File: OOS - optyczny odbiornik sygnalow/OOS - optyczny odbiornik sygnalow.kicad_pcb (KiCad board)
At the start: 2 copper layers, 31 x 47 mm, 55 parts, among them J1 Conn_01x02_Socket, J2 Conn_01x02_Socket, J3 Conn_01x02_Socket, J4 Conn_01x02_Socket, J5 Conn_Coaxial, U1 OPA300AIDBVR, U2 OPA300AIDBVR

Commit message: Creating layout branch, creating a blank pcb file and creating constraints based on JLC PCB capabilities from their website. To every capability lsited a small margin has been added in project constraints (for example if they state min. clearance 0.2mm then in the project that min clearance is 0.3mm
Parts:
- removed C1, C2: 1u, Capacitor_SMD:C_0603_1608Metric
- removed C10, C12: 1p, Capacitor_SMD:C_0402_1005Metric
- removed C11: 100p, Capacitor_SMD:C_0402_1005Metric
- removed C3, C4, C8: 100n, Capacitor_SMD:C_0603_1608Metric
- removed C5, C6, C9: 10n, Capacitor_SMD:C_0402_1005Metric
- removed C7: 2u2, Capacitor_SMD:C_0603_1608Metric
- removed D1, D2: LED, Diode_SMD:D_0603_1608Metric
- removed D3: BPX65, Package_TO_SOT_THT:TO-18-2_Lens
- removed FID1, FID2, FID3: Fiducial, Fiducial:Fiducial_1.5mm_Mask3mm
- removed H1, H2, H3, H4: MountingHole, MountingHole:MountingHole_3.2mm_M3
- removed J1, J2, J3, J4: Conn_01x02_Socket, Connector_PinHeader_2.54mm:PinHeader_1x02_P2.54mm_Vertical
- removed J5: Conn_Coaxial, Connector_Coaxial:BNC_Amphenol_B6252HB-NPP3G-50_Horizontal
- removed JP1: SolderJumper_2_Open, Jumper:SolderJumper-2_P1.3mm_Bridged_RoundedPad1.0x1.5mm
- removed R1: 10k, Resistor_SMD:R_0603_1608Metric
- removed R10, R11, R8: 1k, Resistor_SMD:R_0402_1005Metric
- removed R2: 2k2, Resistor_SMD:R_0603_1608Metric
- removed R3: 10, Resistor_SMD:R_0603_1608Metric
- removed R4, R5, R6, R7: 10k, Resistor_SMD:R_0402_1005Metric
- removed R9: 100, Resistor_SMD:R_0402_1005Metric
- removed REF**: ESD-Logo_6.6x6mm_SilkScreen, Symbol:ESD-Logo_6.6x6mm_SilkScreen
- removed REF**: WEEE-Logo_4.2x6mm_SilkScreen, Symbol:WEEE-Logo_4.2x6mm_SilkScreen
- removed REF**: KiCad-Logo2_5mm_SilkScreen, Symbol:KiCad-Logo2_5mm_SilkScreen
- removed TP1, TP10, TP11, TP2, TP3, TP4, TP5, TP6, TP7, TP8, TP9: TestPoint_Small, TestPoint:TestPoint_Pad_D1.0mm
- removed U1, U2: OPA300AIDBVR, Package_TO_SOT_SMD:SOT-23-6_Handsoldering
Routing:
- net +5V: track 106.5 -> 0.00 mm, vias 2 -> 0
- net /OPA300_En: track 25.1 -> 0.00 mm
- net 0V: track 13.7 -> 0.00 mm, vias 85 -> 0
- net +V_photo: track 9.94 -> 0.00 mm
- net /BPX65_Cathode: track 9.66 -> 0.00 mm
- net /OPA300_TIA_+: track 8.75 -> 0.00 mm
- net /OPA300_TIA_-: track 8.54 -> 0.00 mm
- net /OPA300_En_Alt_Con: track 7.43 -> 0.00 mm
- net /OPA300_x10_Out_AC: track 6.78 -> 0.00 mm
- net /OPA300_x10_-: track 6.58 -> 0.00 mm
- net /OPA300_x10_+: track 5.69 -> 0.00 mm
- net /OPA300_TIA_Out: track 3.95 -> 0.00 mm
- net /OPA300_x10_Out: track 3.47 -> 0.00 mm
- net /OPA300_TIA_Out_AC: track 2.03 -> 0.00 mm
- net Net-(D1-A): track 1.49 -> 0.00 mm
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- removed copper zone on B.Cu, net 0V
- removed copper zone on F.Cu, net 0V
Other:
- board outline removed
- rule pad_to_mask_clearance: 0 -> 0.05
- board text removed: "0"
- board text removed: "0 mm"
- board text removed: "0,01 mm"
- board text removed: "0,02"
- board text removed: "0,035 mm"
- board text removed: "0,1600 mm / 0,1000 mm"
- board text removed: "0,2500 mm"
- board text removed: "1"
- board text removed: "1,51 mm"
- board text removed: "1,6000 mm"
- board text removed: "2"
- board text removed: "3,3"
- board text removed: "31,0000 mm x 47,0000 mm"
- board text removed: "4,5"
- board text removed: "B.Cu"
- board text removed: "B.Mask"
- board text removed: "B.Silkscreen"
- board text removed: "Bottom Silk Screen"
- board text removed: "Bottom Solder Mask"
- board text removed: "CHARAKTERYSTYKA PŁYTKI"
- board text removed: "Całkowity rozmiar płytki:"
- board text removed: "Dielektryk"
- board text removed: "Epsilon R"
- board text removed: "F.Cu"
- board text removed: "F.Mask"
- board text removed: "F.Silkscreen"
- board text removed: "FR4"
- board text removed: "FR4 natural"
- board text removed: "Green"
- board text removed: "Grubość (w mm)"
- board text removed: "Grubość płytki:"
- board text removed: "HAL lead-free"
- board text removed: "Kolor"
- board text removed: "Kontrola impedancji:"
- board text removed: "Liczba warstw sygnałowych:"
- board text removed: "Liquid Ink"
- board text removed: "Liquid Photo"
- board text removed: "Materiał"
- board text removed: "Minimalna ścieżka/odstęp:"
- board text removed: "Minimalna średnica otworu:"
- board text removed: "Nazwa warstwy"
- board text removed: "Nie"
- board text removed: "PRz 05/2025 Rev: 0.0.3"
- board text removed: "Pokrycie brzegu płytki:"
- board text removed: "Pola z kastelacją:"
- board text removed: "Tangens strat"
- board text removed: "Top Silk Screen"
- board text removed: "Top Solder Mask"
- board text removed: "Typ"
- board text removed: "White"
- board text removed: "Wykończenie miedzi:"
- board text removed: "Złącza krawędziowe:"
- board text removed: "copper"
- board text removed: "core"

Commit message: Adding max board dimentions possible to get 2$ PCBs from JLCPCB. Dimentions will be shrunk as the components are being placed
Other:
- board outline added: 100 x 100 mm
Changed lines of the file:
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@@
 				(material "Liquid Photo")
 			)
+			(copper_finish "None")
 			(dielectric_constraints no)
 		)
@@
 			(psa4output no)
 			(plot_black_and_white yes)
+			(plotinvisibletext no)
 			(sketchpadsonfab no)
 			(plotpadnumbers no)
@@
 	(property "Variant" "Master")
 	(net 0 "")
+	(gr_line
+		(start 172.92 119.38)
+		(end 172.92 19.38)
+		(stroke
+			(width 0.05)
+			(type solid)
+		)
+		(layer "Edge.Cuts")
+	)
+	(gr_line
+		(start 172.92 119.38)
+		(end 272.92 119.38)
+		(stroke
+			(width 0.05)
+			(type solid)
+		)
+		(layer "Edge.Cuts")
+	)
+	(gr_line
+		(start 272.92 119.38)
+		(end 272.92 19.38)
+		(stroke
+			(width 0.05)
+			(type solid)
+		)
+		(layer "Edge.Cuts")
+	)
+	(gr_line
+		(start 172.92 19.38)
+		(end 272.92 19.38)
+		(stroke
+			(width 0.05)
+			(type solid)
+		)
+		(layer "Edge.Cuts")
+	)
+	(dimension
+		(type orthogonal)
+		(layer "User.1")
+		(pts
+			(xy 272.92 119.38) (xy 272.92 19.38)
+		)
+		(height 8.5)
+		(orientation 1)
+		(format
+			(prefix "")
+			(suffix "")
+			(units 2)
+			(units_format 1)
+			(precision 2)
+			(suppress_zeroes yes)
+		)
+		(style
+			(thickness 0.1)
+			(arrow_length 1.27)
+			(text_position_mode 0)
+			(arrow_direction outward)
+			(extension_height 0.58642)
+			(extension_offset 0.5)
+			(keep_text_aligned yes)
+		)
+		(gr_text "100 mm"
+			(at 280.27 69.38 90)
+			(layer "User.1")
+			(effects
+				(font
+					(size 1 1)
+					(thickness 0.15)
+				)
+			)
+		)
+	)
+	(dimension
+		(type orthogonal)
+		(layer "User.1")
+		(pts
+			(xy 272.92 119.38) (xy 172.92 119.38)
+		)
+		(height 8)
+		(orientation 0)
+		(format
+			(prefix "")
+			(suffix "")
+			(units 2)
+			(units_format 1)
+			(precision 2)
+			(suppress_zeroes yes)
+		)
+		(style
+			(thickness 0.1)
+			(arrow_length 1.27)
+			(text_position_mode 0)
+			(arrow_direction outward)
+			(extension_height 0.58642)
+			(extension_offset 0.5)
+			(keep_text_aligned yes)
+		)
+		(gr_text "100 mm"
+			(at 222.92 126.23 0)
+			(layer "User.1")
+			(effects
+				(font
+					(size 1 1)
+					(thickness 0.15)
+				)
+			)
+		)
+	)
 	(embedded_fonts no)
 )

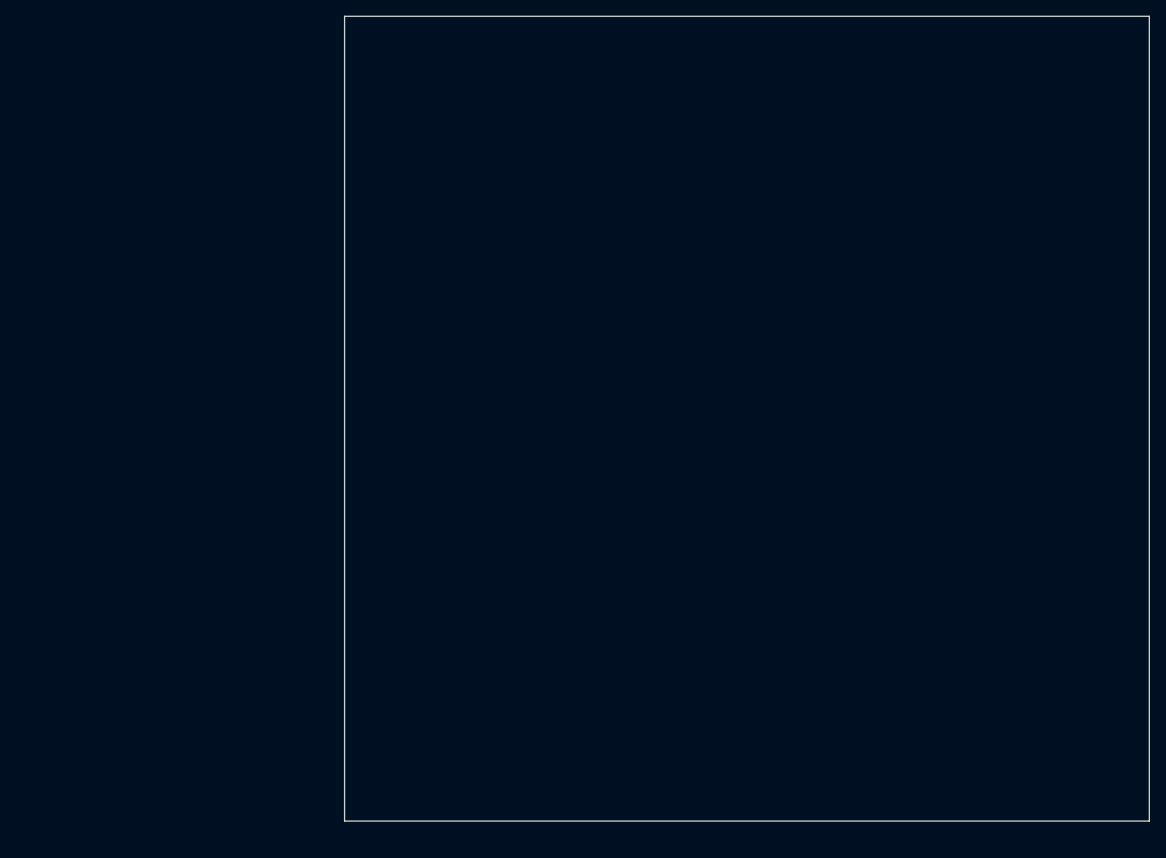
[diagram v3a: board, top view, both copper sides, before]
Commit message: All sections except analog are placed (initial placement) on the PCB. Routing not started yet.
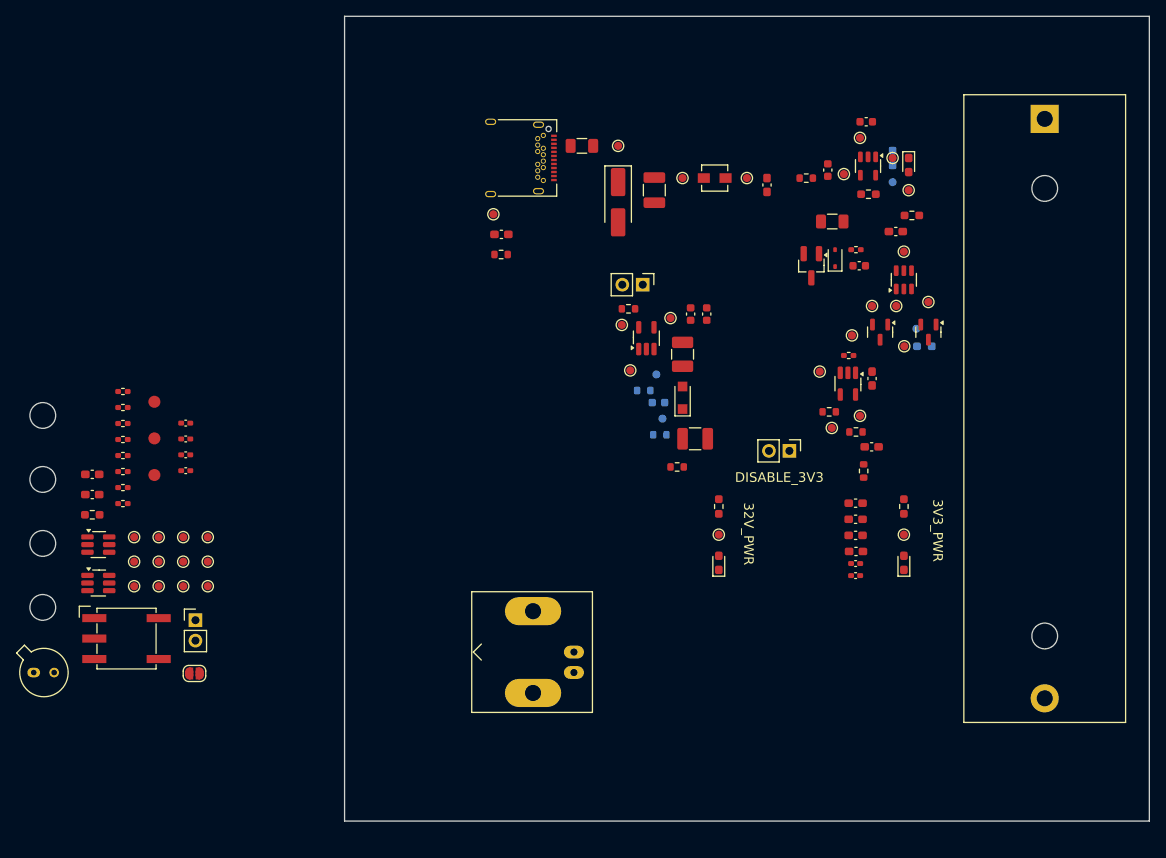
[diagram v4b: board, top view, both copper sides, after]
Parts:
- added BT1: Battery_Cell, Battery:BatteryHolder_MPD_BH-18650-PC2, F.Cu at (259.9, 32.1)
- added C1: 1u, Capacitor_SMD:C_0603_1608Metric_Pad1.08x0.95mm_HandSolder, F.Cu at (236.4, 79.9)
- added C10: 1p, Capacitor_SMD:C_0402_1005Metric_Pad0.74x0.62mm_HandSolder, F.Cu at (153.2, 71.9)
- added C11: 100p, Capacitor_SMD:C_0402_1005Metric_Pad0.74x0.62mm_HandSolder, F.Cu at (153.2, 73.9)
- added C12: 1p, Capacitor_SMD:C_0402_1005Metric_Pad0.74x0.62mm_HandSolder, F.Cu at (153.2, 75.8)
- added C13: 4u7, Capacitor_SMD:C_0603_1608Metric, F.Cu at (215.9, 56.4)
- added C14: 100n, Capacitor_SMD:C_0603_1608Metric, F.Cu at (217.9, 56.4)
- added C15: 10p, Capacitor_SMD:C_0603_1608Metric, B.Cu at (211.9, 67.4)
- added C16: 10u, Capacitor_SMD:C_1210_3225Metric_Pad1.33x2.70mm_HandSolder, F.Cu at (216.5, 71.9)
- added C17: 1u, Capacitor_SMD:C_0603_1608Metric_Pad1.08x0.95mm_HandSolder, F.Cu at (238.5, 64.4)
- added C18: 4u7, Capacitor_SMD:C_0603_1608Metric, F.Cu at (233.0, 38.5)
- added C19: 4u7, Capacitor_SMD:C_0603_1608Metric, F.Cu at (237.7, 32.5)
- added C2: 1u, Capacitor_SMD:C_0603_1608Metric_Pad1.08x0.95mm_HandSolder, F.Cu at (236.4, 81.9)
- added C20: 4u7, Capacitor_SMD:C_0603_1608Metric, F.Cu at (236.9, 50.4)
- added C21: 100n, Capacitor_SMD:C_0603_1608Metric_Pad1.08x0.95mm_HandSolder, F.Cu at (241.4, 46.1)
- added C22: 1u, Capacitor_SMD:C_0603_1608Metric_Pad1.08x0.95mm_HandSolder, F.Cu at (238.4, 72.9)
- added C23: 10u, Capacitor_SMD:C_1210_3225Metric_Pad1.33x2.70mm_HandSolder, F.Cu at (211.4, 41.0)
- added C24: 100n, Capacitor_SMD:C_0603_1608Metric_Pad1.08x0.95mm_HandSolder, F.Cu at (225.4, 40.3)
- added C25: 100n, Capacitor_SMD:C_0603_1608Metric_Pad1.08x0.95mm_HandSolder, F.Cu at (192.4, 46.5)
- added C3: 100n, Capacitor_SMD:C_0603_1608Metric_Pad1.08x0.95mm_HandSolder, F.Cu at (236.4, 83.9)
- added C4: 100n, Capacitor_SMD:C_0603_1608Metric_Pad1.08x0.95mm_HandSolder, F.Cu at (236.5, 85.9)
- added C5: 10n, Capacitor_SMD:C_0402_1005Metric_Pad0.74x0.62mm_HandSolder, F.Cu at (236.4, 87.4)
- added C6: 10n, Capacitor_SMD:C_0402_1005Metric_Pad0.74x0.62mm_HandSolder, F.Cu at (236.4, 88.9)
- added C7: 2u2, Capacitor_SMD:C_0603_1608Metric_Pad1.08x0.95mm_HandSolder, F.Cu at (141.6, 76.3)
- added C8: 100n, Capacitor_SMD:C_0603_1608Metric_Pad1.08x0.95mm_HandSolder, F.Cu at (141.6, 78.8)
- added C9: 10n, Capacitor_SMD:C_0402_1005Metric_Pad0.74x0.62mm_HandSolder, F.Cu at (153.2, 69.9)
- added D1: LED, Diode_SMD:D_0603_1608Metric_Pad1.05x0.95mm_HandSolder, F.Cu at (219.4, 87.3)
- added D2: LED, Diode_SMD:D_0603_1608Metric_Pad1.05x0.95mm_HandSolder, F.Cu at (242.4, 87.3)
- added D3: BPX65, Package_TO_SOT_THT:TO-18-2_Lens, F.Cu at (134.3, 100.9)
- added D4: STPS05, Diode_SMD:Nexperia_CFP3_SOD-123W, F.Cu at (214.9, 66.8)
- added D5: BAT54WSTR, Diode_SMD:D_SOD-323, F.Cu at (233.9, 49.4)
- added D6: LED, Diode_SMD:D_0603_1608Metric_Pad1.05x0.95mm_HandSolder, F.Cu at (243.0, 37.9)
- added D7: SMAJ5.0A-TR, Diode_SMD:D_SMA_Handsoldering, F.Cu at (206.9, 42.5)
- added F1: 0ZCJ0110FF2E, Fuse:Fuse_1206_3216Metric, F.Cu at (202.4, 35.5)
- added F2: 0ZCJ0110FF2E, Fuse:Fuse_1206_3216Metric, F.Cu at (233.5, 44.9)
- added FID1: Fiducial, Fiducial:Fiducial_1.5mm_Mask3mm, F.Cu at (149.3, 67.3)
- added FID2: Fiducial, Fiducial:Fiducial_1.5mm_Mask3mm, F.Cu at (149.3, 71.8)
- added FID3: Fiducial, Fiducial:Fiducial_1.5mm_Mask3mm, F.Cu at (149.3, 76.4)
- added H1: MountingHole, MountingHole:MountingHole_3.2mm_M3, F.Cu at (135.4, 69.0)
- added H2: MountingHole, MountingHole:MountingHole_3.2mm_M3, F.Cu at (135.4, 76.9)
- added H3: MountingHole, MountingHole:MountingHole_3.2mm_M3, F.Cu at (135.4, 84.9)
- added H4: MountingHole, MountingHole:MountingHole_3.2mm_M3, F.Cu at (135.4, 92.8)
- added J1: Conn_01x02_Pin, Connector_PinHeader_2.54mm:PinHeader_1x02_P2.54mm_Vertical, F.Cu at (228.2, 73.4)
- added J4: Conn_01x02_Socket, Connector_PinHeader_2.54mm:PinHeader_1x02_P2.54mm_Vertical, F.Cu at (154.4, 94.4)
- added J5: Conn_Coaxial, Connector_Coaxial:BNC_Amphenol_B6252HB-NPP3G-50_Horizontal, F.Cu at (201.4, 98.4)
- added J6: USB_C_Receptacle, Connector_USB:USB_C_Receptacle_Amphenol_12401548E4-2A, F.Cu at (193.9, 37.0)
- added JP1: SolderJumper_2_Open, Jumper:SolderJumper-2_P1.3mm_Open_RoundedPad1.0x1.5mm, F.Cu at (154.3, 101.0)
- added JP2: 1x2 2.54mm, Connector_PinHeader_2.54mm:PinHeader_1x02_P2.54mm_Vertical, F.Cu at (210.0, 52.7)
- added L1: 10u, Inductor_SMD:L_1210_3225Metric_Pad1.42x2.65mm_HandSolder, F.Cu at (214.9, 61.4)
- added L2: 10u, Inductor_SMD:L_Vishay_IHLP-1212, F.Cu at (218.9, 39.5)
- added Q1: SI2301CDS-T1-GE3, Package_TO_SOT_SMD:SOT-23_Handsoldering, F.Cu at (230.9, 50.4)
- added Q2: AOSS32334C, Package_TO_SOT_SMD:SOT-23, F.Cu at (239.5, 58.6)
- added Q3: AOSS32334C, Package_TO_SOT_SMD:SOT-23, F.Cu at (245.5, 58.6)
- added R1: 10k, Resistor_SMD:R_0603_1608Metric_Pad0.98x0.95mm_HandSolder, F.Cu at (219.4, 80.3)
- added R10: 1k, Resistor_SMD:R_0402_1005Metric_Pad0.72x0.64mm_HandSolder, F.Cu at (145.4, 77.9)
- added R11: 1k, Resistor_SMD:R_0402_1005Metric_Pad0.72x0.64mm_HandSolder, F.Cu at (145.4, 79.9)
- added R12: 0R, Resistor_SMD:R_0603_1608Metric, F.Cu at (237.4, 75.9)
- added R13: 10k, Resistor_SMD:R_0603_1608Metric, F.Cu at (208.2, 55.7)
- added R14: 1M, Resistor_SMD:R_0603_1608Metric, B.Cu at (212.1, 71.4)
- added R15: 40k2, Resistor_SMD:R_0603_1608Metric, B.Cu at (210.1, 65.9)
- added R16: 0R, Resistor_SMD:R_0603_1608Metric, F.Cu at (214.2, 75.4)
- added R17: 2k7, Resistor_SMD:R_0603_1608Metric_Pad0.98x0.95mm_HandSolder, B.Cu at (245.0, 60.4)
- added R18: 330, Resistor_SMD:R_0603_1608Metric_Pad0.98x0.95mm_HandSolder, F.Cu at (243.4, 44.1)
- added R19: 560, Resistor_SMD:R_0603_1608Metric_Pad0.98x0.95mm_HandSolder, F.Cu at (238.0, 41.5)
- added R2: 2k2, Resistor_SMD:R_0603_1608Metric_Pad0.98x0.95mm_HandSolder, F.Cu at (242.4, 80.3)
- added R20: 2k, Resistor_SMD:R_0603_1608Metric_Pad0.98x0.95mm_HandSolder, B.Cu at (241.0, 37.0)
- added R21: 10k, Resistor_SMD:R_0402_1005Metric_Pad0.72x0.64mm_HandSolder, F.Cu at (236.5, 48.4)
- added R22: 10k, Resistor_SMD:R_0402_1005Metric_Pad0.72x0.64mm_HandSolder, F.Cu at (235.6, 61.5)
- added R23: 40k2, Resistor_SMD:R_0603_1608Metric, F.Cu at (236.5, 71.0)
- added R24: 24k3, Resistor_SMD:R_0603_1608Metric, F.Cu at (233.1, 68.5)
- added R25: 0R, Resistor_SMD:R_0603_1608Metric, F.Cu at (230.3, 39.5)
- added R26: 330R, Resistor_SMD:R_0603_1608Metric, F.Cu at (192.4, 49.0)
- added R3: 10, Resistor_SMD:R_0603_1608Metric_Pad0.98x0.95mm_HandSolder, F.Cu at (141.6, 81.3)
- added R4: 10k, Resistor_SMD:R_0402_1005Metric_Pad0.72x0.64mm_HandSolder, F.Cu at (145.4, 66.0)
- added R5: 10k, Resistor_SMD:R_0402_1005Metric_Pad0.72x0.64mm_HandSolder, F.Cu at (145.4, 68.0)
- added R6: 10k, Resistor_SMD:R_0402_1005Metric_Pad0.72x0.64mm_HandSolder, F.Cu at (145.4, 70.0)
- added R7: 10k, Resistor_SMD:R_0402_1005Metric_Pad0.72x0.64mm_HandSolder, F.Cu at (145.4, 72.0)
- added R8: 1k, Resistor_SMD:R_0402_1005Metric_Pad0.72x0.64mm_HandSolder, F.Cu at (145.4, 74.0)
- added R9: 100, Resistor_SMD:R_0402_1005Metric_Pad0.72x0.64mm_HandSolder, F.Cu at (145.4, 76.0)
- added SW1: SW_Rotary_1x8_MP, Button_Switch_SMD:Nidec_Copal_SH-7040B, F.Cu at (145.8, 96.7)
- added TP1: TestPoint_Small, TestPoint:TestPoint_Pad_D1.0mm, F.Cu at (146.8, 84.1)
- added TP10: TestPoint_Small, TestPoint:TestPoint_Pad_D1.0mm, F.Cu at (155.9, 84.1)
- added TP11: TestPoint_Small, TestPoint:TestPoint_Pad_D1.0mm, F.Cu at (155.9, 87.2)
- added TP12: TestPoint_Small, TestPoint:TestPoint_Pad_D1.0mm, F.Cu at (213.4, 56.9)
- added TP13: TestPoint_Small, TestPoint:TestPoint_Pad_D1.0mm, F.Cu at (208.4, 63.4)
- added TP14: TestPoint_Small, TestPoint:TestPoint_Pad_D1.0mm, B.Cu at (212.4, 69.4)
- added TP15: TestPoint_Small, TestPoint:TestPoint_Pad_D1.0mm, B.Cu at (211.7, 63.9)
- added TP16: TestPoint_Small, TestPoint:TestPoint_Pad_D1.0mm, F.Cu at (207.4, 57.7)
- added TP17: TestPoint_Small, TestPoint:TestPoint_Pad_D1.0mm, F.Cu at (219.4, 83.8)
- added TP18: TestPoint_Small, TestPoint:TestPoint_Pad_D1.0mm, F.Cu at (235.0, 39.0)
- added TP19: TestPoint_Small, TestPoint:TestPoint_Pad_D1.0mm, F.Cu at (243.0, 41.0)
- added TP2: TestPoint_Small, TestPoint:TestPoint_Pad_D1.0mm, F.Cu at (146.8, 87.2)
- added TP20: TestPoint_Small, TestPoint:TestPoint_Pad_D1.0mm, F.Cu at (241.0, 37.0)
- added TP21: TestPoint_Small, TestPoint:TestPoint_Pad_D1.0mm, F.Cu at (237.0, 34.5)
- added TP22: TestPoint_Small, TestPoint:TestPoint_Pad_D1.0mm, B.Cu at (241.0, 40.0)
- added TP23: TestPoint_Small, TestPoint:TestPoint_Pad_D1.0mm, F.Cu at (238.5, 55.4)
- added TP24: TestPoint_Small, TestPoint:TestPoint_Pad_D1.0mm, F.Cu at (242.4, 48.6)
- added TP25: TestPoint_Small, TestPoint:TestPoint_Pad_D1.0mm, B.Cu at (244.0, 58.2)
- added TP26: TestPoint_Small, TestPoint:TestPoint_Pad_D1.0mm, F.Cu at (242.5, 60.4)
- added TP27: TestPoint_Small, TestPoint:TestPoint_Pad_D1.0mm, F.Cu at (241.5, 55.4)
- added TP28: TestPoint_Small, TestPoint:TestPoint_Pad_D1.0mm, F.Cu at (245.5, 54.9)
- added TP29: TestPoint_Small, TestPoint:TestPoint_Pad_D1.0mm, F.Cu at (236.0, 59.0)
- added TP3: TestPoint_Small, TestPoint:TestPoint_Pad_D1.0mm, F.Cu at (146.8, 90.2)
- added TP30: TestPoint_Small, TestPoint:TestPoint_Pad_D1.0mm, F.Cu at (232.0, 63.5)
- added TP31: TestPoint_Small, TestPoint:TestPoint_Pad_D1.0mm, F.Cu at (233.5, 70.5)
- added TP32: TestPoint_Small, TestPoint:TestPoint_Pad_D1.0mm, F.Cu at (237.0, 69.0)
- added TP33: TestPoint_Small, TestPoint:TestPoint_Pad_D1.0mm, F.Cu at (242.4, 83.8)
- added TP34: TestPoint_Small, TestPoint:TestPoint_Pad_D1.0mm, F.Cu at (155.9, 90.2)
- added TP35: TestPoint_Small, TestPoint:TestPoint_Pad_D1.0mm, F.Cu at (214.9, 39.5)
- added TP36: TestPoint_Small, TestPoint:TestPoint_Pad_D1.0mm, F.Cu at (222.9, 39.5)
- added TP37: TestPoint_Small, TestPoint:TestPoint_Pad_D1.0mm, F.Cu at (206.9, 35.5)
- added TP38: TestPoint_Small, TestPoint:TestPoint_Pad_D1.0mm, F.Cu at (191.4, 44.0)
- added TP4: TestPoint_Small, TestPoint:TestPoint_Pad_D1.0mm, F.Cu at (149.8, 84.1)
- added TP5: TestPoint_Small, TestPoint:TestPoint_Pad_D1.0mm, F.Cu at (149.8, 87.2)
- added TP6: TestPoint_Small, TestPoint:TestPoint_Pad_D1.0mm, F.Cu at (149.8, 90.2)
- added TP7: TestPoint_Small, TestPoint:TestPoint_Pad_D1.0mm, F.Cu at (152.9, 84.1)
- added TP8: TestPoint_Small, TestPoint:TestPoint_Pad_D1.0mm, F.Cu at (152.9, 87.2)
- added TP9: TestPoint_Small, TestPoint:TestPoint_Pad_D1.0mm, F.Cu at (152.9, 90.2)
- added U1: OPA300AIDBVR, Package_TO_SOT_SMD:SOT-23-6_Handsoldering, F.Cu at (142.3, 85.0)
- added U2: OPA300AIDBVR, Package_TO_SOT_SMD:SOT-23-6_Handsoldering, F.Cu at (142.3, 89.8)
- added U3: AP3015KTR-G1, Package_TO_SOT_SMD:SOT-23-5_HandSoldering, F.Cu at (210.4, 59.4)
- added U4: MCP73831T-2ATI/OT, Package_TO_SOT_SMD:SOT-23-5, F.Cu at (238.0, 38.0)
- added U5: AP9101CAK6-ANTRG1, Package_TO_SOT_SMD:SOT-23-6, F.Cu at (242.4, 52.1)
- added U6: AP2126K-ADJTRG1, Package_TO_SOT_SMD:SOT-23-5_HandSoldering, F.Cu at (235.5, 65.0)
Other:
- board text added: "32V_PWR"
- board text added: "3V3_PWR"
- board text added: "Analog com."
- board text added: "Battery com."
- board text added: "DCDC com."
- board text added: "DISABLE_3V3"
- board text added: "TODO: - !! Connect rotary switch (SW1) !!"
- board text added: "USB com."

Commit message: Initial component placement is done. Rotary switch needs to be added and a 4th mount hole placed or removed (to be decided). When selecting resistors for the rotary switch please consider 0402 case due to limited space left on the PCB
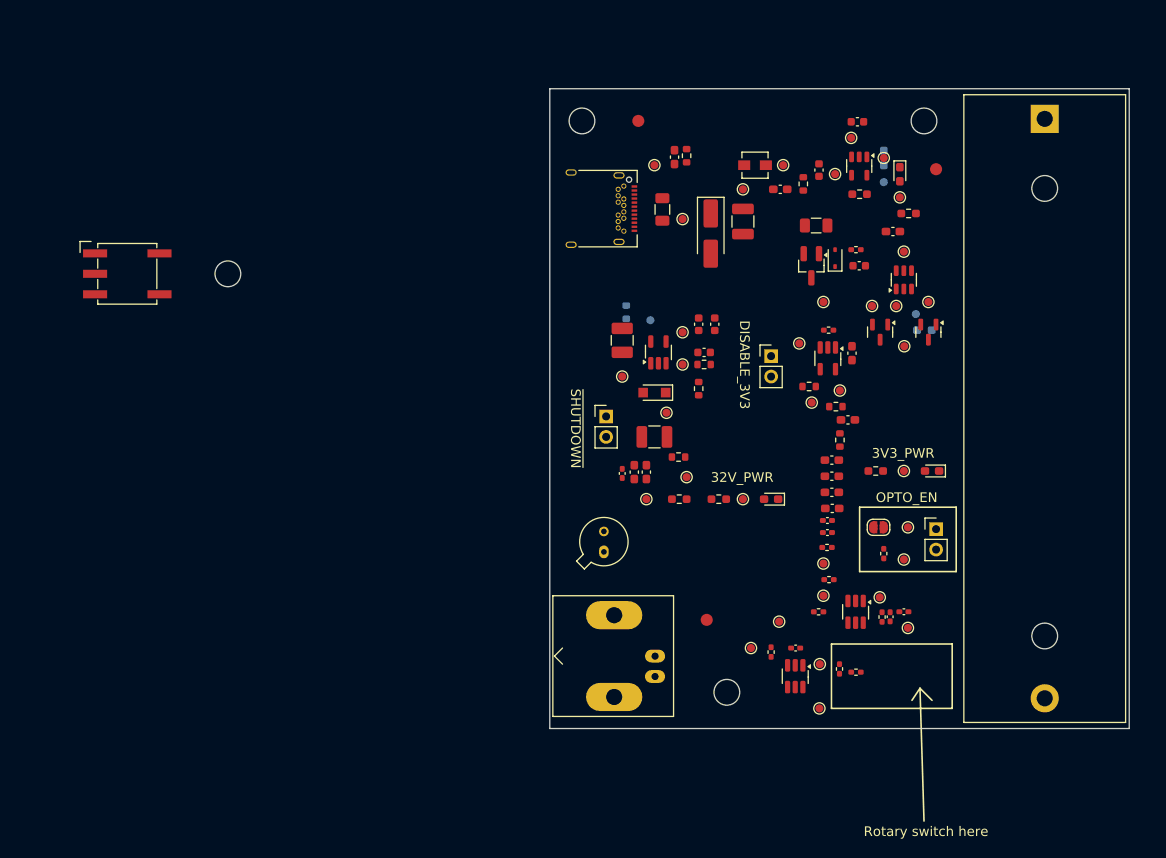
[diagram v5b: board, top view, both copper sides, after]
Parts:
- C15, R14, R15, TP14, TP15: moved to F.Cu
- R13, TP16: moved to B.Cu
- moved H2 118.2 mm to (244.9, 32.4)
- moved FID2 102.7 mm to (246.4, 38.4)
- moved R4 96.7 mm to (239.9, 86.1), turned to -90 degrees
- moved R8 96.4 mm to (239.7, 94.0), turned to 90 degrees
- moved U1 94.5 mm to (236.4, 93.4), turned to -90 degrees
- moved R9 94.4 mm to (236.5, 100.9), turned to 180 degrees
- moved J4 92.7 mm to (246.4, 83.1)
- moved TP5 92.6 mm to (242.4, 86.9)
- moved R10 91.8 mm to (234.4, 100.5), turned to 90 degrees
- moved C11 91.3 mm to (242.4, 93.4)
- moved TP8 90.4 mm to (242.9, 95.4), turned to 90 degrees
- moved C10 90.3 mm to (240.7, 94.0), turned to 90 degrees
- moved R6 89.9 mm to (233.1, 89.4), turned to 180 degrees
- moved R5 89.2 mm to (232.9, 85.4), turned to 180 degrees
- moved R7 89.1 mm to (231.8, 93.4), turned to 180 degrees
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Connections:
- R1 pad 1: Net-(D4-K) -> +32V
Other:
- board size 100 x 100 mm -> 72 x 79.5 mm
- board text added: "OPTO_EN"
- board text added: "Rotary switch here"
- board text added: "TODO: - !! Connect rotary switch (SW1) !! - place the 4th MH"
- board text added: "~{SHUTDOWN}"
- board text removed: "Analog com."
- board text removed: "Battery com."
- board text removed: "DCDC com."
- board text removed: "TODO: - !! Connect rotary switch (SW1) !!"
- board text removed: "USB com."
